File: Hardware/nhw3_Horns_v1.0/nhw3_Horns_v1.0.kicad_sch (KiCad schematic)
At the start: 0 parts

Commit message: Horns Board Spec Sheet
Finished 1st revision of Horns Board Spec Sheet. Followed wiki instructions, will ask for some clarification on tuesday to update sheet.
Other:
- title: Template -> Horns Board
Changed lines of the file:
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@@
-(kicad_sch (version 20211123) (generator eeschema)
-  (paper "USLetter")
-  (title_block
-    (title "Template")
-    (date "2022-08-16")
-    (rev "0.0")
-    (company "Illini Solar Car")
-    (comment 1 "Designed By: Your Name")
-  )
-  (sheet_instances
-    (path "/" (page "1"))
-  )
+(kicad_sch
+	(version 20231120)
+	(generator "eeschema")
+	(generator_version "8.0")
+	(paper "USLetter")
+	(title_block
+		(title "Horns Board")
+		(date "2022-08-16")
+		(rev "1.0")
+		(company "Illini Solar Car")
+		(comment 1 "Designed By: Nathan Wang")
+	)
+	(sheet_instances
+		(path "/"
+			(page "1")
+		)
+	)
 )

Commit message: HornsBoard Schematic Rev1
Finished first revision of schematic and passed ERC. Need to organize and format neater. Also still need to assign footprints.
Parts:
- added C1, C2, C3, C4, C5: 0.1μF, symbol device:C
- added C10: 100μF, symbol Device:C_Polarized_US
- added C6, C7: 1μF, symbol device:C
- added C8, C9: 10μF, symbol device:C
- added D1: D, symbol Device:D
- added F1, F2: 2A, symbol Device:Fuse
- added J1: Conn_01x03, symbol Connector_Generic:Conn_01x03
- added J2, J3, J4: Conn_01x02, symbol Connector_Generic:Conn_01x02
- added Q1: Q_NMOS_GDS, symbol device:Q_NMOS_GDS
- added R1, R2: 1kΩ, symbol Device:R_US
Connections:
- new net: C10.2, C3.2, C4.2, C5.2, C6.2, C7.2, C8.2, C9.2
- new net: F2.1, R2.2
- new net: F1.1, Q1.2 (D)
- new net: J3.1 (Pin_1), J4.2 (Pin_2)
- new net: C1.1, R1.2
- new net: C1.2, Q1.3 (S)
- new net: C2.2, R2.1
- new net: C2.1, Q1.1 (G)
- new net +24V: C10.1, C3.1, C4.1, C5.1, C6.1, C7.1, C8.1, C9.1, D1.2 (A), J1.2 (Pin_2), J3.2 (Pin_2)
- new net GND: J1.1 (Pin_1), J1.3 (Pin_3), J2.1 (Pin_1), R1.1
- new net HORN_CTRL: F2.2, J2.2 (Pin_2)
- new net HORN_IN: D1.1 (K), F1.2, J4.1 (Pin_1)

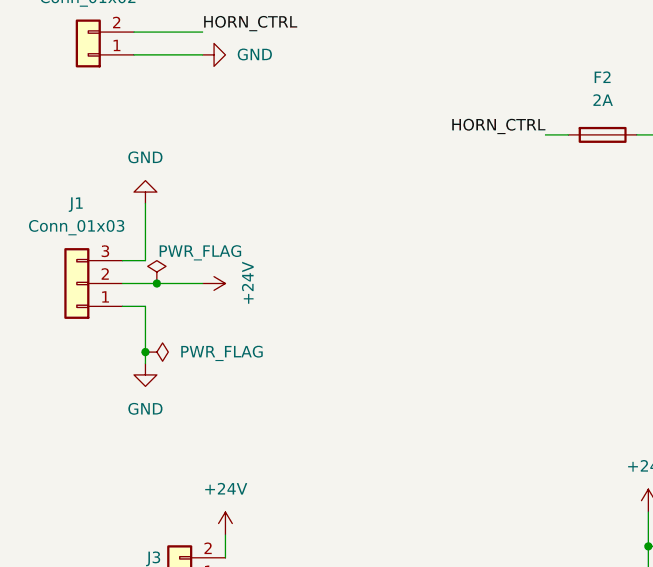
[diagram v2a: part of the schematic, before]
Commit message: Assigned Horns Board Footprints
Finished assigning horns boards footprints for diodes, capacitors, resistors, MOSFET, and connectors. Also updated datasheet links for MOSFET and connectors. Passed ERC again.
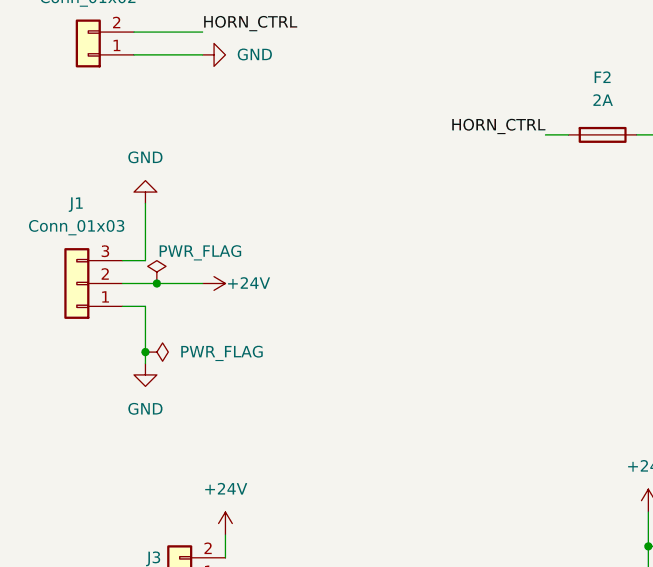
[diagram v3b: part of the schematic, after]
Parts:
- C1, C10, C2, C3, C4, C5, C6, C7, C8, C9: footprint (none) -> Capacitor_SMD:C_0603_1608Metric_Pad1.08x0.95mm_HandSolder
- D1: footprint (none) -> Diode_SMD:D_0603_1608Metric_Pad1.05x0.95mm_HandSolder
- F1, F2: footprint (none) -> Fuse:Fuse_0603_1608Metric_Pad1.05x0.95mm_HandSolder
- J1: footprint (none) -> Connector_Molex:Molex_KK-254_AE-6410-03A_1x03_P2.54mm_Vertical; MPN (none) -> 0022272031
- J2, J3, J4: footprint (none) -> Connector_Molex:Molex_KK-254_AE-6410-02A_1x02_P2.54mm_Vertical; MPN (none) -> 022272021
- Q1: footprint (none) -> layout:TO-252-2; MPN (none) -> IRFR010PBF
- R1, R2: footprint (none) -> Resistor_SMD:R_0603_1608Metric_Pad0.98x0.95mm_HandSolder

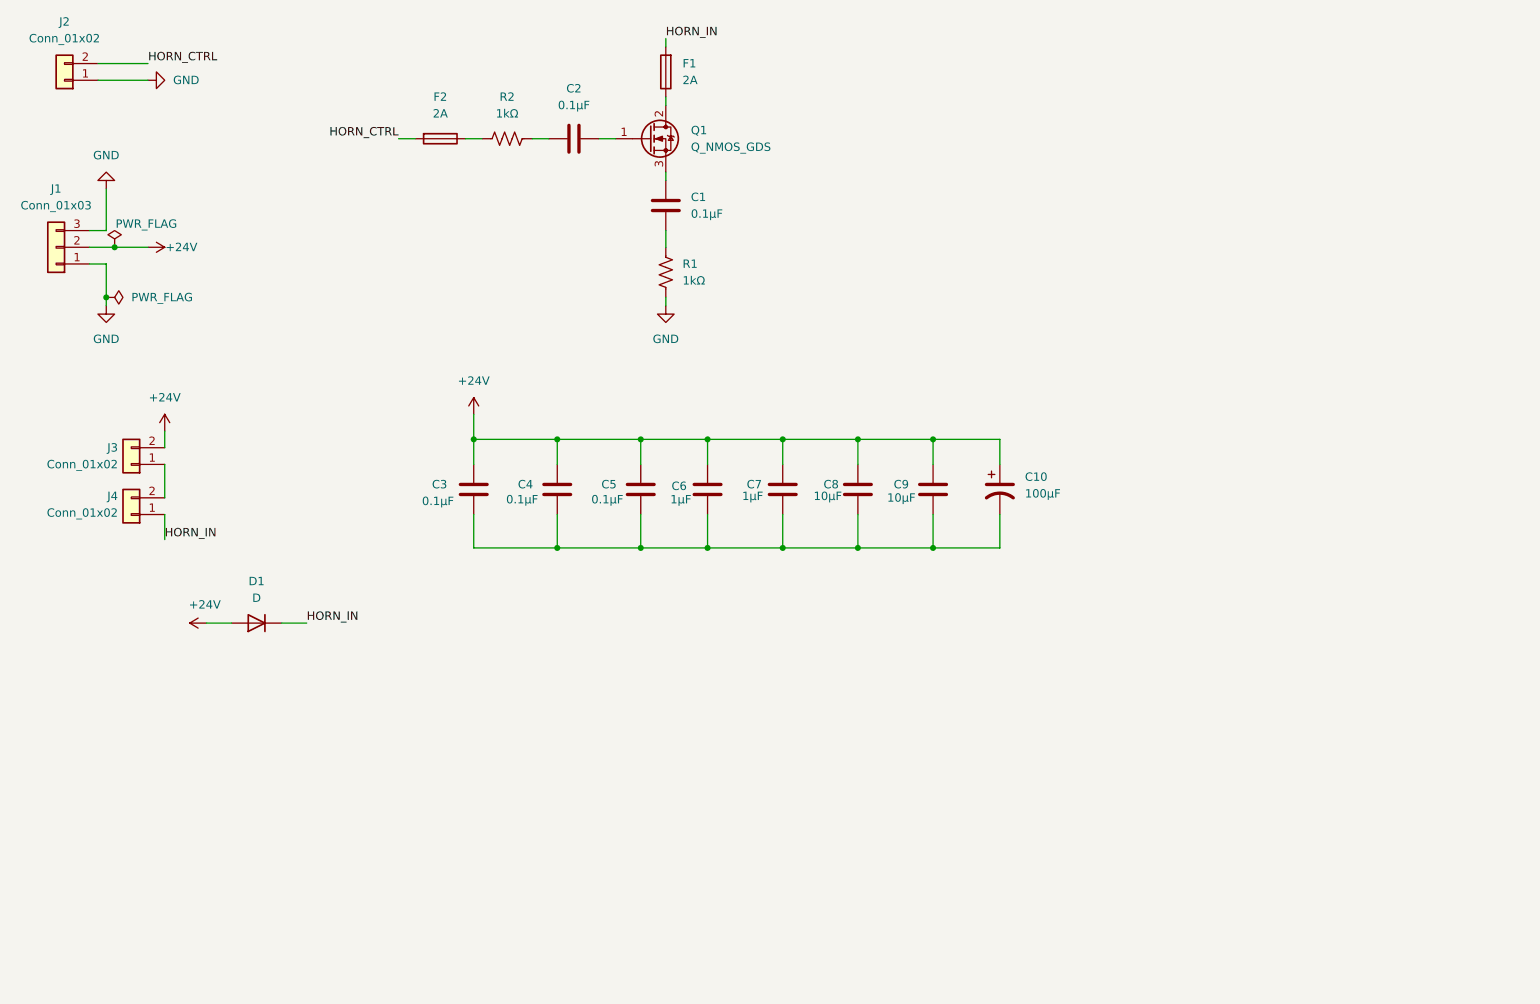
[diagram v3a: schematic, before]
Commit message: Cleaned Up Horns Board
Added boxes and titles to label different parts of horns board schematic. Passed ERC with 0 errors.
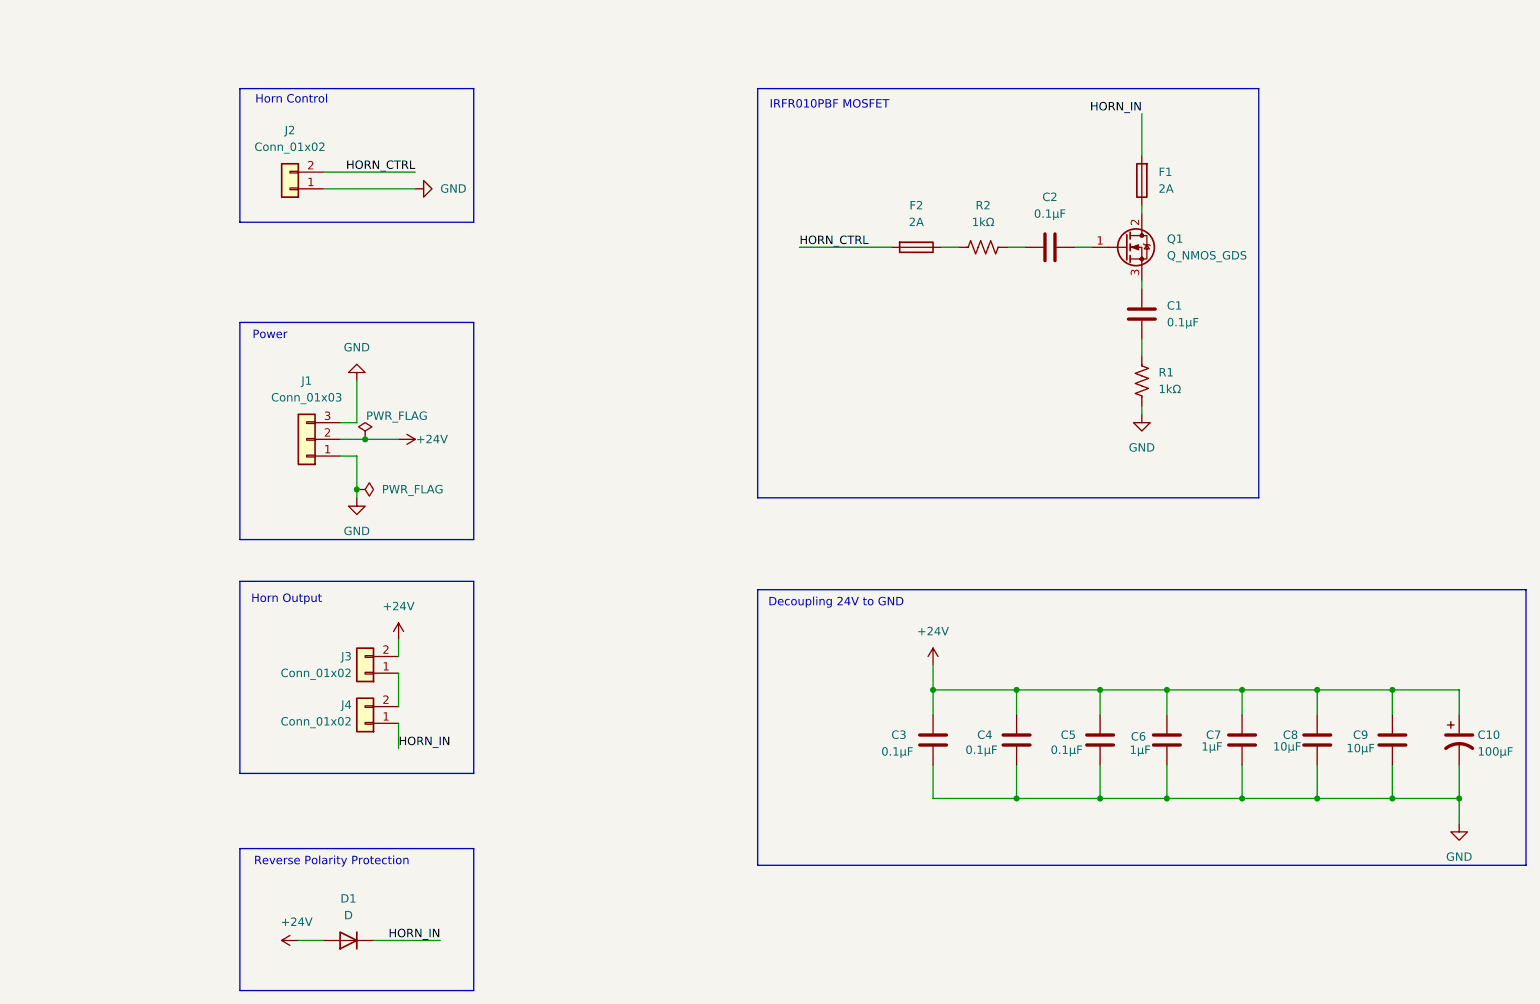
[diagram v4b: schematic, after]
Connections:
- net GND: now also C10.2, C3.2, C4.2, C5.2, C6.2, C7.2, C8.2, C9.2
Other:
- note added: "Decoupling 24V to GND"
- note added: "Horn Control"
- note added: "Horn Output"
- note added: "IRFR010PBF MOSFET"
- note added: "Power"
- note added: "Reverse Polarity Protection"
- moved on the sheet: C1, C10, C2, C3, C4, C5, C6, C7, C8, C9, D1, F1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

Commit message: Finished Horns Board Layout
Fixed half-first order RC filter on MOSFET, finished PCB layout. Ran DRC with no errors.
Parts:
- removed C1: 0.1μF, Capacitor_SMD:C_0603_1608Metric_Pad1.08x0.95mm_HandSolder, symbol device:C
- removed F2: 2A, Fuse:Fuse_0603_1608Metric_Pad1.05x0.95mm_HandSolder, symbol Device:Fuse
- removed R1: 1kΩ, Resistor_SMD:R_0603_1608Metric_Pad0.98x0.95mm_HandSolder, symbol Device:R_US
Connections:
- net GND: now also C2.2, Q1.3 (S), R2.2
- net HORN_CTRL: now also C2.1, Q1.1 (G), R2.1
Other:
- note added: "Half First Order RC Filter"
- moved on the sheet: C2, R2

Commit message: Added push button to debug horns board
Added a push button in horns board schematic, assigned footprint, and updated pcb layout. Passed DRC with 0 errors.
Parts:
- added SW1: SW_Push, Button_Switch_SMD:SW_Push_1P1T_NO_CK_KMR2, symbol Switch:SW_Push
- D1: MPN (none) -> ES2DA-13-F
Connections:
- net GND: now also SW1.2
- net at F1.1, Q1.2 (D): now also SW1.1
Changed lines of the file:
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@@
+	)
+	(junction
+		(at 189.23 46.99)
+		(diameter 0)
+		(color 0 0 0 0)
 	)
 	(junction
@@
 	)
 	(junction
+		(at 189.23 60.96)
+		(diameter 0)
+		(color 0 0 0 0)
+	)
+	(junction
 		(at 193.04 120.65)
 		(diameter 0)
@@
 	(wire
 		(pts
+			(xy 189.23 46.99) (xy 210.82 46.99)
+		)
+		(stroke
+			(width 0)
+			(type default)
+		)
+	)
+	(wire
+		(pts
 			(xy 157.48 120.65) (xy 157.48 124.46)
 		)
@@
 	(wire
 		(pts
+			(xy 189.23 60.96) (xy 210.82 60.96)
+		)
+		(stroke
+			(width 0)
+			(type default)
+		)
+	)
+	(wire
+		(pts
 			(xy 67.31 82.55) (xy 71.12 82.55)
 		)
@@
 	(wire
 		(pts
-			(xy 189.23 58.42) (xy 189.23 63.5)
+			(xy 189.23 58.42) (xy 189.23 60.96)
 		)
 		(stroke
@@
 	(wire
 		(pts
+			(xy 210.82 60.96) (xy 210.82 58.42)
+		)
+		(stroke
+			(width 0)
+			(type default)
+		)
+	)
+	(wire
+		(pts
+			(xy 189.23 60.96) (xy 189.23 63.5)
+		)
+		(stroke
+			(width 0)
+			(type default)
+		)
+	)
+	(wire
+		(pts
 			(xy 204.47 132.08) (xy 204.47 137.16)
 		)
@@
 		(pts
 			(xy 69.85 85.09) (xy 69.85 90.17)
+		)
+		(stroke
+			(width 0)
+			(type default)
+		)
+	)
+	(wire
+		(pts
+			(xy 210.82 46.99) (xy 210.82 48.26)
 		)
 		(stroke
@@
 	(rectangle
 		(start 130.81 29.21)
-		(end 207.01 91.44)
+		(end 224.79 91.44)
 		(stroke
 			(width 0)
@@
 			)
 		)
-		(property "Datasheet" "~"
+		(property "Datasheet" "https://www.diodes.com/assets/Datasheets/ds14002.pdf"
 			(at 68.58 158.75 0)
 			(effects
@@
 			)
 		)
-		(property "MPN" ""
+		(property "MPN" "ES2DA-13-F"
 			(at 68.58 158.75 0)
 			(effects
@@
 					(unit 1)
 				)
+			)
+		)
+	)
+	(symbol
+		(lib_id "Switch:SW_Push")
+		(at 210.82 53.34 270)
+		(unit 1)
+		(exclude_from_sim no)
+		(in_bom yes)
+		(on_board yes)
+		(dnp no)
+		(fields_autoplaced yes)
+		(property "Reference" "SW1"
+			(at 214.63 52.0699 90)
+			(effects
+				(font
+					(size 1.27 1.27)
+				)
+				(justify left)
+			)
+		)
+		(property "Value" "SW_Push"
+			(at 214.63 54.6099 90)
+			(effects
+				(font
+					(size 1.27 1.27)
+				)
+				(justify left)
+			)
+		)
+		(property "Footprint" "Button_Switch_SMD:SW_Push_1P1T_NO_CK_KMR2"
+			(at 215.9 53.34 0)
+			(effects
+				(font
+					(size 1.27 1.27)
+				)
+				(hide yes)
+			)
+		)
+		(property "Datasheet" "~"
+			(at 215.9 53.34 0)
+			(effects
+				(font
+					(size 1.27 1.27)
+				)
+				(hide yes)
+			)
+		)
+		(property "Description" "Push button switch, generic, two pins"
+			(at 210.82 53.34 0)
+			(effects
+				(font
+					(size 1.27 1.27)
+				)
+				(hide yes)
+			)
+		)
+		(pin "2"
+		)
+		(pin "1"
+		)
+		(instances
+			(project ""
+				(path "/1e1b062d-fad0-427c-a622-c5b8a80b5268"
+					(reference "SW1")
+					(unit 1)
+				)

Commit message: Updated Connector Footprints
Changed from KK254 to Molex Micro-Fit Connector footprints. Updated layout as well, passed DRC with no errors or warnings.
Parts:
- J1: footprint Connector_Molex:Molex_KK-254_AE-6410-03A_1x03_P2.54mm_Vertical -> Connector_Molex:Molex_Micro-Fit_3.0_43650-0300_1x03_P3.00mm_Horizontal
- J2, J3, J4: footprint Connector_Molex:Molex_KK-254_AE-6410-02A_1x02_P2.54mm_Vertical -> Connector_Molex:Molex_Micro-Fit_3.0_43650-0200_1x02_P3.00mm_Horizontal
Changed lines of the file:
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@@
 			)
 		)
-		(property "Footprint" "Connector_Molex:Molex_KK-254_AE-6410-03A_1x03_P2.54mm_Vertical"
+		(property "Footprint" "Connector_Molex:Molex_Micro-Fit_3.0_43650-0300_1x03_P3.00mm_Horizontal"
 			(at 62.23 82.55 0)
 			(effects
@@
 			)
 		)
-		(property "Footprint" "Connector_Molex:Molex_KK-254_AE-6410-02A_1x02_P2.54mm_Vertical"
+		(property "Footprint" "Connector_Molex:Molex_Micro-Fit_3.0_43650-0200_1x02_P3.00mm_Horizontal"
 			(at 59.69 44.45 0)
 			(effects
@@
 			)
 		)
-		(property "Footprint" "Connector_Molex:Molex_KK-254_AE-6410-02A_1x02_P2.54mm_Vertical"
+		(property "Footprint" "Connector_Molex:Molex_Micro-Fit_3.0_43650-0200_1x02_P3.00mm_Horizontal"
 			(at 71.12 125.73 0)
 			(effects
@@
 			)
 		)
-		(property "Footprint" "Connector_Molex:Molex_KK-254_AE-6410-02A_1x02_P2.54mm_Vertical"
+		(property "Footprint" "Connector_Molex:Molex_Micro-Fit_3.0_43650-0200_1x02_P3.00mm_Horizontal"
 			(at 71.12 118.11 0)
 			(effects
